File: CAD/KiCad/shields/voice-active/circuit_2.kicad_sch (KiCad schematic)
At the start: 14 parts

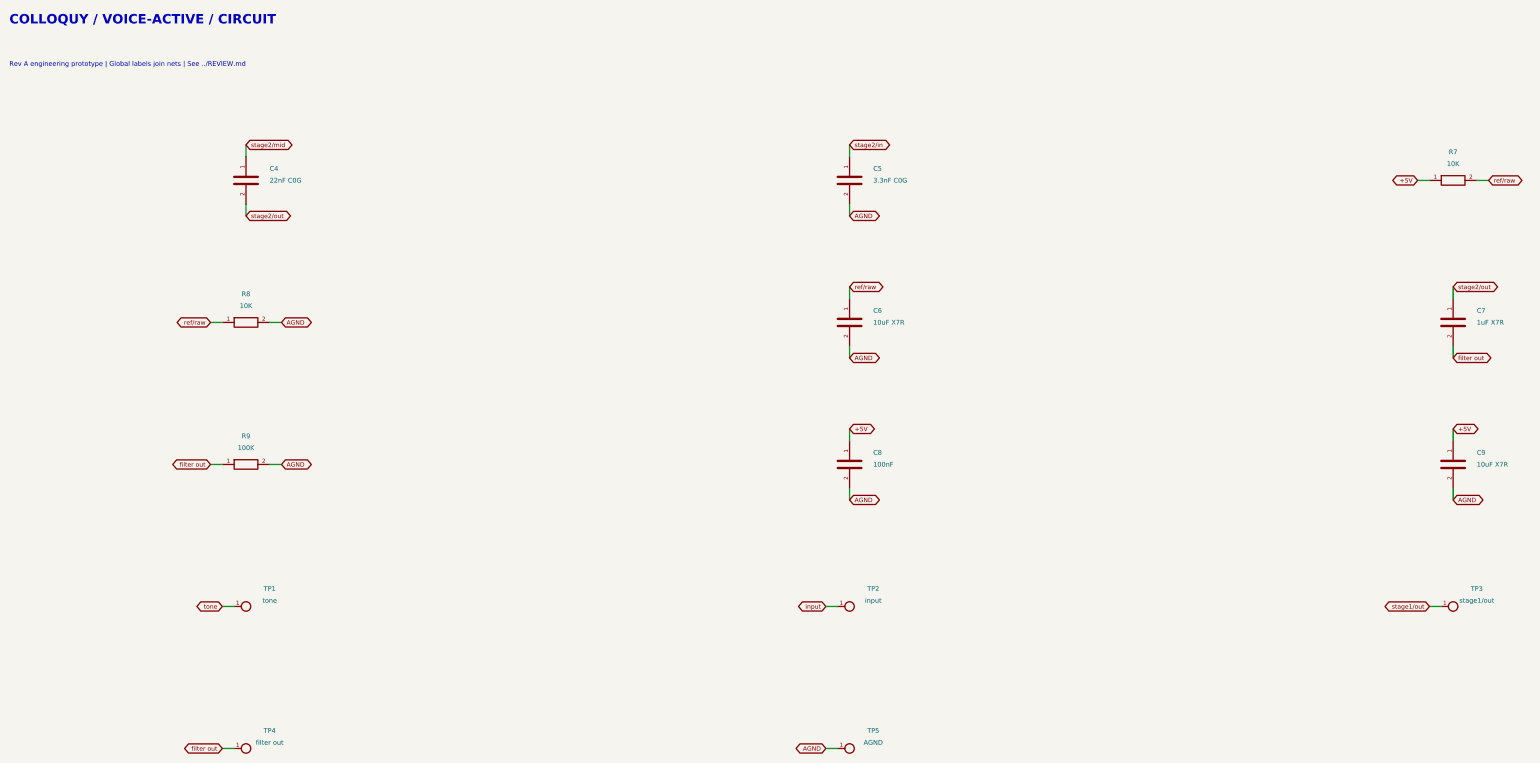
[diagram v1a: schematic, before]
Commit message: Remove shield identification and adopt the simplified connector and Teensy pin maps
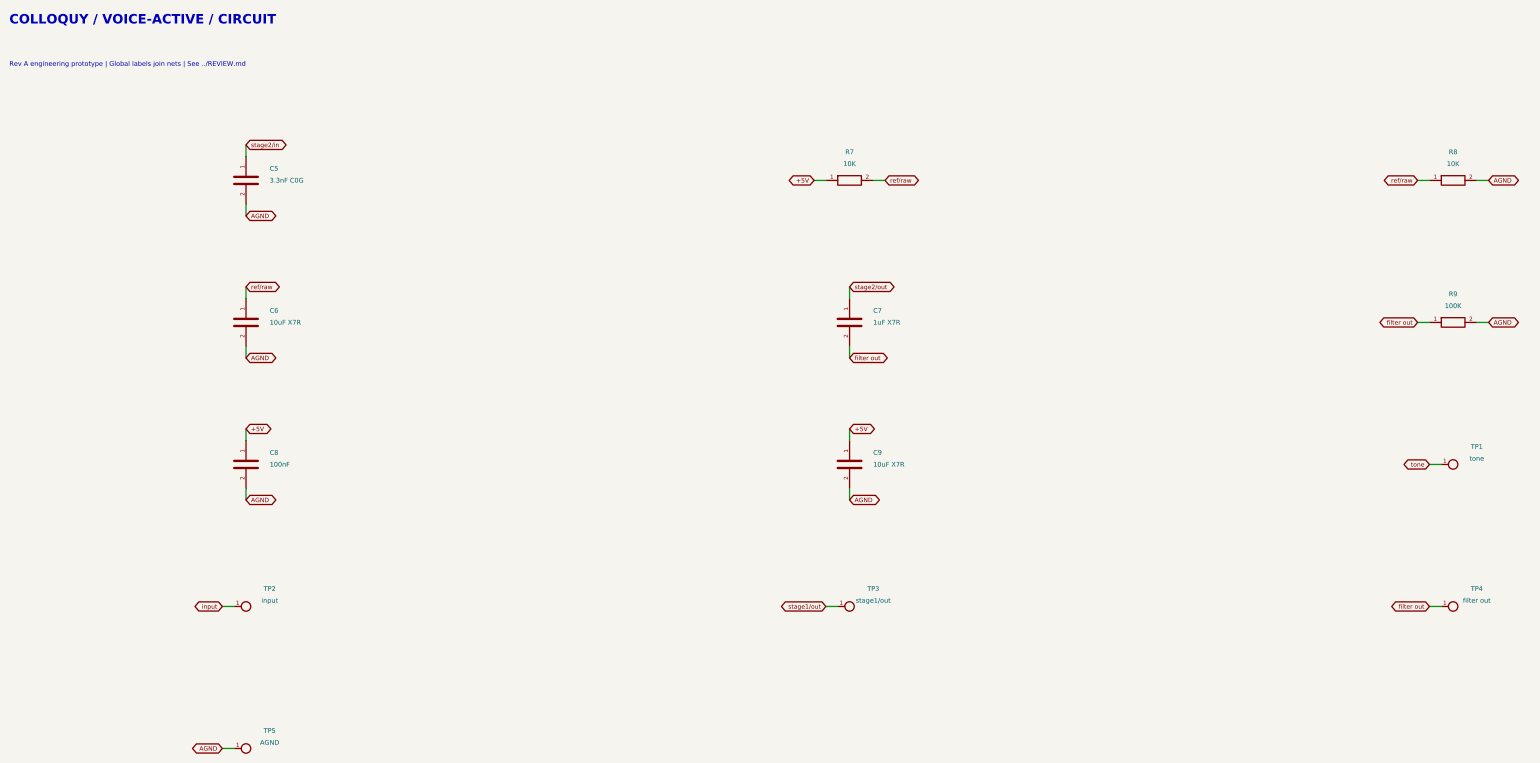
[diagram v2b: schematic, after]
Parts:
- removed C4: 22nF C0G, Shields:C_0805_2012Metric, symbol Colloquy:C4
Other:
- moved on the sheet: C5, C6, C7, C8, C9, R7, R8, R9, TP1, TP2, TP3, TP4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

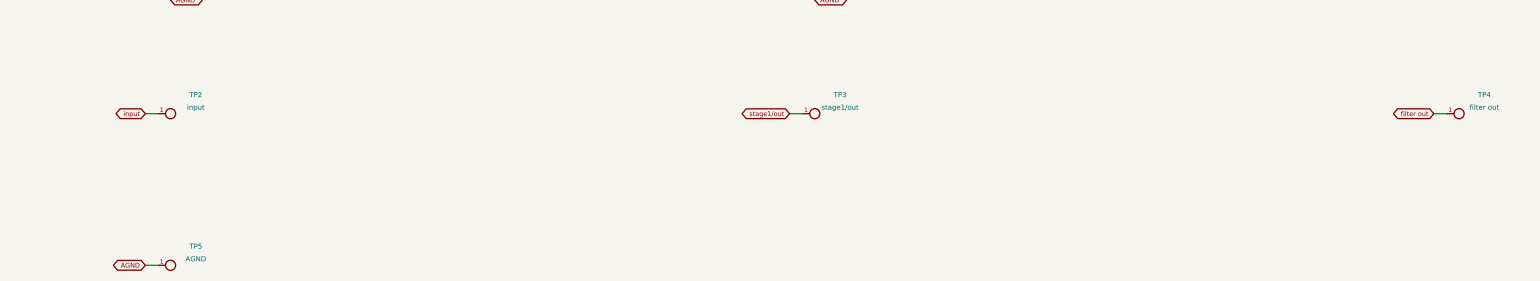
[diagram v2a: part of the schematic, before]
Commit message: Finish revised shield routing, printed identification and clean KiCad checks
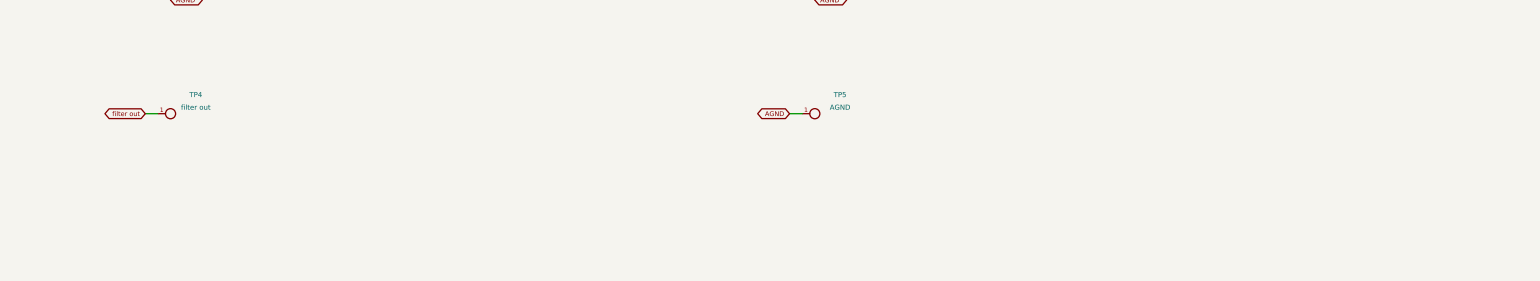
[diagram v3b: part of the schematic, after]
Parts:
- removed TP2: input, Shields:TestPoint_Pad_D1.5mm, symbol Colloquy:TP2
- removed TP3: stage1/out, Shields:TestPoint_Pad_D1.5mm, symbol Colloquy:TP3
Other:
- moved on the sheet: TP4, TP5
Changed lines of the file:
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@@
 (wire (pts (xy 322.5800 111.7600) (xy 320.0400 111.7600)) (stroke (width 0) (type default)))
 (global_label "tone" (shape bidirectional) (at 320.0400 111.7600 180) (effects (font (size 0.95 0.95)) (justify right)) (property "Intersheetrefs" "${INTERSHEET_REFS}" (at 320.0400 111.7600 0) (effects (font (size 1.016 1.016))  (hide yes))))
-(symbol (lib_id "Colloquy:TP2") (at 66.0400 142.2400 0) (unit 1) (exclude_from_sim no) (in_bom no) (on_board yes) (dnp no)
-(property "Reference" "TP2" (at 71.1200 138.4300 0) (effects (font (size 1.016 1.016))  ))
-(property "Value" "input" (at 71.1200 140.9700 0) (effects (font (size 1.016 1.016))  ))
+(symbol (lib_id "Colloquy:TP4") (at 66.0400 142.2400 0) (unit 1) (exclude_from_sim no) (in_bom no) (on_board yes) (dnp no)
+(property "Reference" "TP4" (at 71.1200 138.4300 0) (effects (font (size 1.016 1.016))  ))
+(property "Value" "filter out" (at 71.1200 140.9700 0) (effects (font (size 1.016 1.016))  ))
 (property "Footprint" "Shields:TestPoint_Pad_D1.5mm" (at 66.0400 142.2400 0) (effects (font (size 1.27 1.27))  (hide yes)))
 (property "Datasheet" "" (at 66.0400 142.2400 0) (effects (font (size 1.27 1.27))  (hide yes)))
 (property "Description" "" (at 66.0400 142.2400 0) (effects (font (size 1.27 1.27))  (hide yes)))
 (pin "1")
-(instances (project "voice-active" (path "/6ab3a972-ce0c-5353-96b8-6900f2ada186/5b035efa-76de-5941-a005-132a6c1edd19" (reference "TP2") (unit 1)))))
+(instances (project "voice-active" (path "/6ab3a972-ce0c-5353-96b8-6900f2ada186/5b035efa-76de-5941-a005-132a6c1edd19" (reference "TP4") (unit 1)))))
 (wire (pts (xy 63.5000 142.2400) (xy 60.9600 142.2400)) (stroke (width 0) (type default)))
-(global_label "input" (shape bidirectional) (at 60.9600 142.2400 180) (effects (font (size 0.95 0.95)) (justify right)) (property "Intersheetrefs" "${INTERSHEET_REFS}" (at 60.9600 142.2400 0) (effects (font (size 1.016 1.016))  (hide yes))))
-(symbol (lib_id "Colloquy:TP3") (at 195.5800 142.2400 0) (unit 1) (exclude_from_sim no) (in_bom no) (on_board yes) (dnp no)
-(property "Reference" "TP3" (at 200.6600 138.4300 0) (effects (font (size 1.016 1.016))  ))
-(property "Value" "stage1/out" (at 200.6600 140.9700 0) (effects (font (size 1.016 1.016))  ))
+(global_label "filter out" (shape bidirectional) (at 60.9600 142.2400 180) (effects (font (size 0.95 0.95)) (justify right)) (property "Intersheetrefs" "${INTERSHEET_REFS}" (at 60.9600 142.2400 0) (effects (font (size 1.016 1.016))  (hide yes))))
+(symbol (lib_id "Colloquy:TP5") (at 195.5800 142.2400 0) (unit 1) (exclude_from_sim no) (in_bom no) (on_board yes) (dnp no)
+(property "Reference" "TP5" (at 200.6600 138.4300 0) (effects (font (size 1.016 1.016))  ))
+(property "Value" "AGND" (at 200.6600 140.9700 0) (effects (font (size 1.016 1.016))  ))
 (property "Footprint" "Shields:TestPoint_Pad_D1.5mm" (at 195.5800 142.2400 0) (effects (font (size 1.27 1.27))  (hide yes)))
 (property "Datasheet" "" (at 195.5800 142.2400 0) (effects (font (size 1.27 1.27))  (hide yes)))
 (property "Description" "" (at 195.5800 142.2400 0) (effects (font (size 1.27 1.27))  (hide yes)))
 (pin "1")
-(instances (project "voice-active" (path "/6ab3a972-ce0c-5353-96b8-6900f2ada186/5b035efa-76de-5941-a005-132a6c1edd19" (reference "TP3") (unit 1)))))
+(instances (project "voice-active" (path "/6ab3a972-ce0c-5353-96b8-6900f2ada186/5b035efa-76de-5941-a005-132a6c1edd19" (reference "TP5") (unit 1)))))
 (wire (pts (xy 193.0400 142.2400) (xy 190.5000 142.2400)) (stroke (width 0) (type default)))
-(global_label "stage1/out" (shape bidirectional) (at 190.5000 142.2400 180) (effects (font (size 0.95 0.95)) (justify right)) (property "Intersheetrefs" "${INTERSHEET_REFS}" (at 190.5000 142.2400 0) (effects (font (size 1.016 1.016))  (hide yes))))
-(symbol (lib_id "Colloquy:TP4") (at 325.1200 142.2400 0) (unit 1) (exclude_from_sim no) (in_bom no) (on_board yes) (dnp no)
-(property "Reference" "TP4" (at 330.2000 138.4300 0) (effects (font (size 1.016 1.016))  ))
-(property "Value" "filter out" (at 330.2000 140.9700 0) (effects (font (size 1.016 1.016))  ))
-(property "Footprint" "Shields:TestPoint_Pad_D1.5mm" (at 325.1200 142.2400 0) (effects (font (size 1.27 1.27))  (hide yes)))
-(property "Datasheet" "" (at 325.1200 142.2400 0) (effects (font (size 1.27 1.27))  (hide yes)))
-(property "Description" "" (at 325.1200 142.2400 0) (effects (font (size 1.27 1.27))  (hide yes)))
-(pin "1")
-(instances (project "voice-active" (path "/6ab3a972-ce0c-5353-96b8-6900f2ada186/5b035efa-76de-5941-a005-132a6c1edd19" (reference "TP4") (unit 1)))))
-(wire (pts (xy 322.5800 142.2400) (xy 320.0400 142.2400)) (stroke (width 0) (type default)))
-(global_label "filter out" (shape bidirectional) (at 320.0400 142.2400 180) (effects (font (size 0.95 0.95)) (justify right)) (property "Intersheetrefs" "${INTERSHEET_REFS}" (at 320.0400 142.2400 0) (effects (font (size 1.016 1.016))  (hide yes))))
-(symbol (lib_id "Colloquy:TP5") (at 66.0400 172.7200 0) (unit 1) (exclude_from_sim no) (in_bom no) (on_board yes) (dnp no)
-(property "Reference" "TP5" (at 71.1200 168.9100 0) (effects (font (size 1.016 1.016))  ))
-(property "Value" "AGND" (at 71.1200 171.4500 0) (effects (font (size 1.016 1.016))  ))
-(property "Footprint" "Shields:TestPoint_Pad_D1.5mm" (at 66.0400 172.7200 0) (effects (font (size 1.27 1.27))  (hide yes)))
-(property "Datasheet" "" (at 66.0400 172.7200 0) (effects (font (size 1.27 1.27))  (hide yes)))
-(property "Description" "" (at 66.0400 172.7200 0) (effects (font (size 1.27 1.27))  (hide yes)))
-(pin "1")
-(instances (project "voice-active" (path "/6ab3a972-ce0c-5353-96b8-6900f2ada186/5b035efa-76de-5941-a005-132a6c1edd19" (reference "TP5") (unit 1)))))
-(wire (pts (xy 63.5000 172.7200) (xy 60.9600 172.7200)) (stroke (width 0) (type default)))
-(global_label "AGND" (shape bidirectional) (at 60.9600 172.7200 180) (effects (font (size 0.95 0.95)) (justify right)) (property "Intersheetrefs" "${INTERSHEET_REFS}" (at 60.9600 172.7200 0) (effects (font (size 1.016 1.016))  (hide yes))))
+(global_label "AGND" (shape bidirectional) (at 190.5000 142.2400 180) (effects (font (size 0.95 0.95)) (justify right)) (property "Intersheetrefs" "${INTERSHEET_REFS}" (at 190.5000 142.2400 0) (effects (font (size 1.016 1.016))  (hide yes))))
           (embedded_fonts no))
